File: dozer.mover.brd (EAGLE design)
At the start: 84.8 x 55.9 mm, 10 parts, among them IC1 PIC18F4550_40, U1 L298, U2 L298

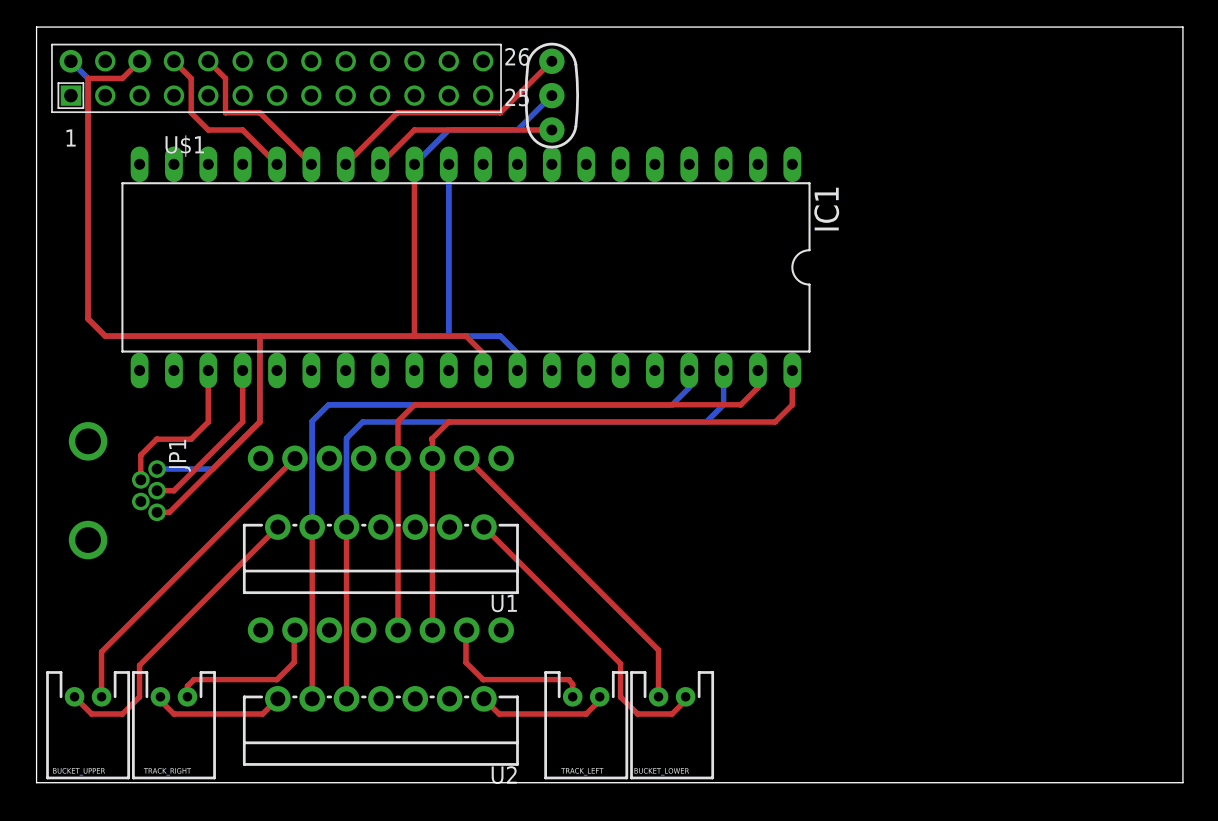
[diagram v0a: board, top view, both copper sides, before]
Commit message: Updated Board to be more elegant
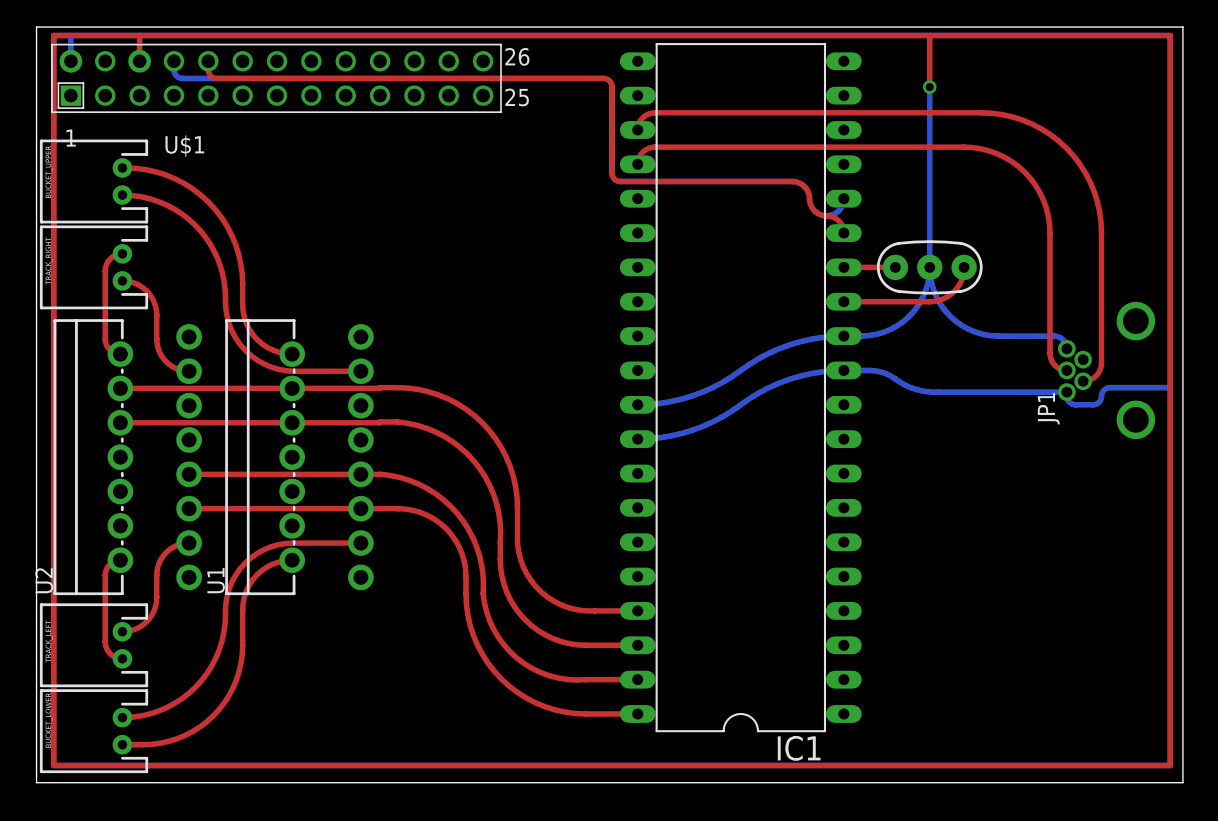
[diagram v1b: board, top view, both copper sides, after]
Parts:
- moved JP1 78.0 mm to (81.3, 30.5), turned to 180 degrees
- moved BUCKET_LOWER 40.7 mm to (6.35, 3.81), turned to 90 degrees
- moved BUCKET_UPPER 38.2 mm to (6.35, 44.5), turned to 90 degrees
- moved TRACK_LEFT 34.5 mm to (6.35, 10.2), turned to 90 degrees
- moved TRACK_RIGHT 32.0 mm to (6.35, 38.1), turned to 90 degrees
- moved Y1 30.7 mm to (66.0, 38.1), turned to 0 degrees
- moved U2 22.5 mm to (8.89, 24.1), turned to 90 degrees
- moved IC1 22.2 mm to (52.1, 29.2), turned to 90 degrees
- moved U1 4.58 mm to (21.6, 24.1), turned to 90 degrees
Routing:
- net 5VDC: track 81.7 -> 316.5 mm
- net GND: track 95.3 -> 329.3 mm, vias 0 -> 1
- net UARTTX: track 12.3 -> 58.9 mm
- net UARTRX: track 12.3 -> 56.3 mm
- net USB-: track 11.6 -> 50.0 mm
- net USB+: track 12.2 -> 44.3 mm
- net OSC2: track 18.4 -> 3.81 mm
- net CHAN1-: track 44.4 -> 39.5 mm
- net CHAN2+: track 50.7 -> 46.3 mm
- net CHAN2-: track 50.7 -> 46.4 mm
- net CHAN1+: track 44.4 -> 40.2 mm
- net OSC1: track 13.8 -> 9.94 mm
- net BKTU-: track 22.6 -> 19.1 mm
- net TRKL-: track 11.9 -> 8.60 mm
- net TRKR+: track 11.8 -> 8.72 mm
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
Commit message: Renamed parts at Mhisani's behest
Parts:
- J1: value RASPBERRY-PI -> (none)
- renumbered U$1 to J1
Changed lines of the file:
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@@
 </autorouter>
 <elements>
-<element name="U$1" library="RaspberryPi" package="RASPBERRY-PI" value="RASPBERRY-PI" x="2.54" y="50.8"/>
+<element name="J1" library="RaspberryPi" package="RASPBERRY-PI" value="" x="2.54" y="50.8"/>
 <element name="IC1" library="microchip" package="DIL40" value="PIC18F4550_40" x="52.07" y="29.21" rot="R90">
 <attribute name="OC_NEWARK" value="74K8623" x="125.73" y="68.58" size="1.778" layer="27" rot="R90" display="off"/>
@@
 <signal name="GND">
 <contactref element="Y1" pad="2"/>
-<contactref element="U$1" pad="6"/>
+<contactref element="J1" pad="6"/>
 <contactref element="IC1" pad="12"/>
 <contactref element="IC1" pad="31"/>
@@
 </signal>
 <signal name="5VDC">
-<contactref element="U$1" pad="2"/>
+<contactref element="J1" pad="2"/>
 <contactref element="IC1" pad="11"/>
 <contactref element="IC1" pad="32"/>
@@
 </signal>
 <signal name="UARTTX">
-<contactref element="U$1" pad="8"/>
+<contactref element="J1" pad="8"/>
 <contactref element="IC1" pad="16"/>
 <wire x1="10.16" y1="53.34" x2="10.16" y2="52.705" width="0.4064" layer="16"/>
@@
 </signal>
 <signal name="UARTRX">
-<contactref element="U$1" pad="10"/>
+<contactref element="J1" pad="10"/>
 <contactref element="IC1" pad="15"/>
 <wire x1="41.91" y1="52.07" x2="42.545" y2="51.435" width="0.4064" layer="1" curve="-90"/>

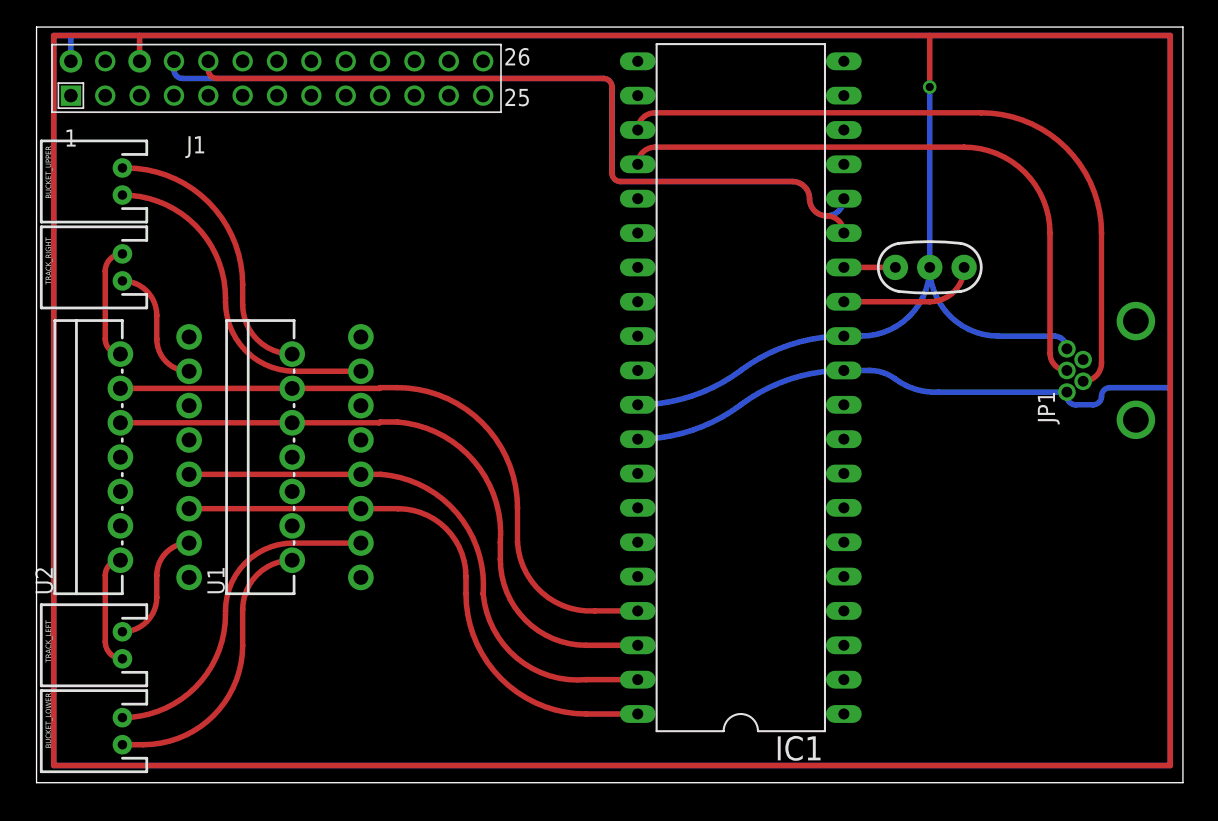
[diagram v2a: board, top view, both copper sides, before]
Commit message: Added beefy 5v vreg for both internal supply and powering the Raspberry Pi
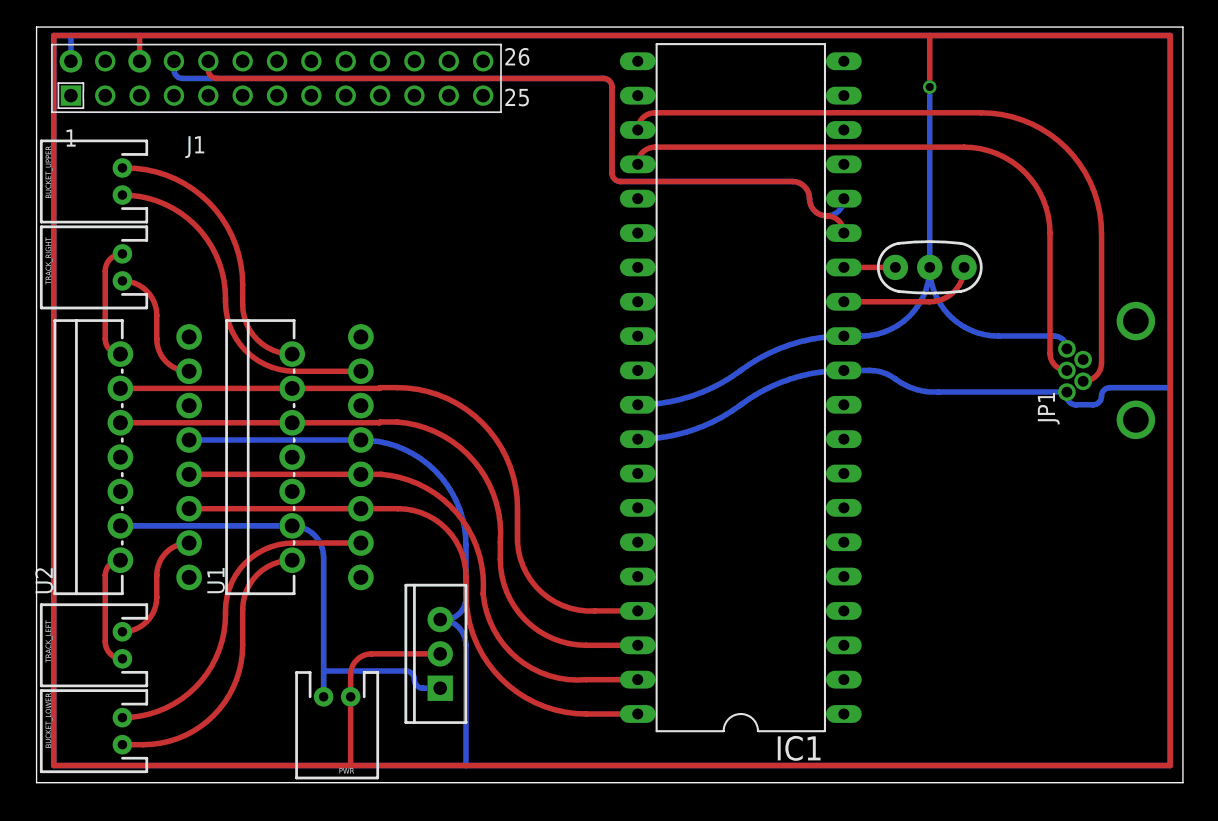
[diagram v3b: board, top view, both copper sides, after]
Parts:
- added IC2: (no value), SparkFun-PowerIC:TO220-IGO
- added PWR: (no value), SparkFun-Connectors:JST-2-PTH
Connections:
- removed net N$21: U1.9
- removed net N$22: U1.4
- removed net N$29: U2.9
- removed net N$30: U2.4
- new net V_RAW: IC2.IN, PWR.2, U1.4, U2.4
- net 5VDC: now also IC2.OUT, U1.9, U2.9
- net GND: now also IC2.GND, PWR.1
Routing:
- net 5VDC: track 316.5 -> 358.2 mm
- net V_RAW: track 0.00 -> 35.4 mm
- net GND: track 329.3 -> 343.2 mm
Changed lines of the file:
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@@
 <setting verticaltext="up"/>
 </settings>
-<grid distance="0.025" unitdist="inch" unit="inch" style="dots" multiple="1" display="yes" altdistance="0.025" altunitdist="inch" altunit="mm"/>
+<grid distance="0.0125" unitdist="inch" unit="inch" style="dots" multiple="1" display="yes" altdistance="0.025" altunitdist="inch" altunit="mm"/>
 <layers>
 <layer number="1" name="Top" color="4" fill="1" visible="yes" active="yes"/>
@@
 <element name="BUCKET_LOWER" library="SparkFun-Connectors" package="JST-2-PTH" value="" x="6.35" y="3.81" rot="R90"/>
 <element name="BUCKET_UPPER" library="SparkFun-Connectors" package="JST-2-PTH" value="" x="6.35" y="44.45" rot="R90"/>
+<element name="PWR" library="SparkFun-Connectors" package="JST-2-PTH" value="" x="22.225" y="6.35" rot="R180"/>
+<element name="IC2" library="SparkFun-PowerIC" package="TO220-IGO" value="" x="29.845" y="9.525" rot="R90"/>
 </elements>
 <signals>
@@
 <wire x1="66.04" y1="55.245" x2="83.82" y2="55.245" width="0.4064" layer="1"/>
 <wire x1="83.82" y1="55.245" x2="83.82" y2="1.27" width="0.4064" layer="1"/>
-<wire x1="83.82" y1="1.27" x2="1.27" y2="1.27" width="0.4064" layer="1"/>
+<wire x1="83.82" y1="1.27" x2="23.225" y2="1.27" width="0.4064" layer="1"/>
+<wire x1="23.225" y1="1.27" x2="1.27" y2="1.27" width="0.4064" layer="1"/>
 <wire x1="1.27" y1="1.27" x2="1.27" y2="55.245" width="0.4064" layer="1"/>
 <wire x1="1.27" y1="55.245" x2="7.62" y2="55.245" width="0.4064" layer="1"/>
@@
 <via x="66.04" y="51.435" extent="1-16" drill="0.6" shape="square"/>
 <wire x1="66.04" y1="51.435" x2="66.04" y2="38.1" width="0.4064" layer="16"/>
+<contactref element="PWR" pad="1"/>
+<wire x1="23.225" y1="6.35" x2="23.225" y2="1.27" width="0.4064" layer="1"/>
+<contactref element="IC2" pad="GND"/>
+<wire x1="23.225" y1="6.35" x2="23.225" y2="7.985" width="0.4064" layer="1"/>
+<wire x1="23.225" y1="7.985" x2="24.765" y2="9.525" width="0.4064" layer="1" curve="-90"/>
+<wire x1="24.765" y1="9.525" x2="29.845" y2="9.525" width="0.4064" layer="1"/>
 </signal>
 <signal name="5VDC">
@@
 <wire x1="83.82" y1="55.245" x2="83.82" y2="29.21" width="0.4064" layer="16"/>
 <wire x1="83.82" y1="29.21" x2="83.82" y2="1.27" width="0.4064" layer="16"/>
-<wire x1="83.82" y1="1.27" x2="1.27" y2="1.27" width="0.4064" layer="16"/>
+<wire x1="83.82" y1="1.27" x2="31.75" y2="1.27" width="0.4064" layer="16"/>
+<wire x1="31.75" y1="1.27" x2="1.27" y2="1.27" width="0.4064" layer="16"/>
 <wire x1="1.27" y1="1.27" x2="1.27" y2="55.245" width="0.4064" layer="16"/>
 <wire x1="1.27" y1="55.245" x2="2.54" y2="55.245" width="0.4064" layer="16"/>
@@
 <wire x1="61.595" y1="30.48" x2="63.5" y2="29.845" width="0.4064" layer="16" curve="-36.869898"/>
 <wire x1="63.5" y1="29.845" x2="66.675" y2="28.88" width="0.4064" layer="16" curve="39.927839"/>
+<contactref element="U2" pad="9"/>
+<contactref element="U1" pad="9"/>
+<contactref element="IC2" pad="OUT"/>
+<wire x1="29.845" y1="12.065" x2="31.75" y2="10.16" width="0.4064" layer="16" curve="-90"/>
+<wire x1="31.75" y1="10.16" x2="31.75" y2="1.27" width="0.4064" layer="16"/>
+<wire x1="23.98" y1="25.34" x2="11.28" y2="25.34" width="0.4064" layer="16"/>
+<wire x1="23.98" y1="25.34" x2="31.75" y2="17.57" width="0.4064" layer="16" curve="-90"/>
+<wire x1="31.75" y1="17.57" x2="31.75" y2="13.6525" width="0.4064" layer="16"/>
+<wire x1="29.845" y1="12.065" x2="30.1625" y2="12.065" width="0.4064" layer="16"/>
+<wire x1="30.1625" y1="12.065" x2="31.75" y2="13.6525" width="0.4064" layer="16" curve="90"/>
 </signal>
 <signal name="USB+">
@@
 <contactref element="U1" pad="6"/>
 </signal>
-<signal name="N$21">
-<contactref element="U1" pad="9"/>
-</signal>
-<signal name="N$22">
-<contactref element="U1" pad="4"/>
-</signal>
 <signal name="N$23">
 <contactref element="U1" pad="1"/>
@@
 <signal name="N$28">
 <contactref element="U2" pad="6"/>
-</signal>
-<signal name="N$29">
-<contactref element="U2" pad="9"/>
-</signal>
-<signal name="N$30">
-<contactref element="U2" pad="4"/>
 </signal>
 <signal name="N$7">
@@
 <wire x1="13.335" y1="52.07" x2="41.91" y2="52.07" width="0.4064" layer="1"/>
 </signal>
+<signal name="V_RAW">
+<contactref element="PWR" pad="2"/>
+<contactref element="U1" pad="4"/>
+<contactref element="U2" pad="4"/>
+<wire x1="21.225" y1="6.35" x2="21.225" y2="8.255" width="0.4064" layer="16"/>
+<wire x1="21.225" y1="8.255" x2="21.225" y2="16.665" width="0.4064" layer="16"/>
+<wire x1="21.225" y1="16.665" x2="18.9" y2="18.99" width="0.4064" layer="16" curve="90"/>
+<wire x1="18.9" y1="18.99" x2="6.2" y2="18.99" width="0.4064" layer="16"/>
+<contactref element="IC2" pad="IN"/>
+<wire x1="29.845" y1="6.985" x2="28.575" y2="6.985" width="0.4064" layer="16"/>
+<wire x1="28.575" y1="6.985" x2="27.94" y2="7.62" width="0.4064" layer="16" curve="-90"/>
+<wire x1="27.94" y1="7.62" x2="27.305" y2="8.255" width="0.4064" layer="16" curve="90"/>
+<wire x1="27.305" y1="8.255" x2="21.225" y2="8.255" width="0.4064" layer="16"/>
+</signal>
 </signals>
